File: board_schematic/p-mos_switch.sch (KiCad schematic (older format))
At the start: 5 parts

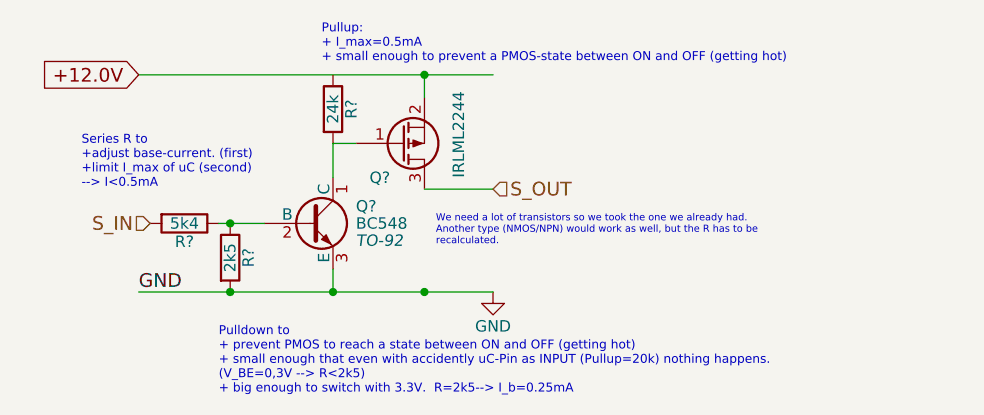
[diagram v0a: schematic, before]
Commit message: V0.2.1: First schematic for BOM
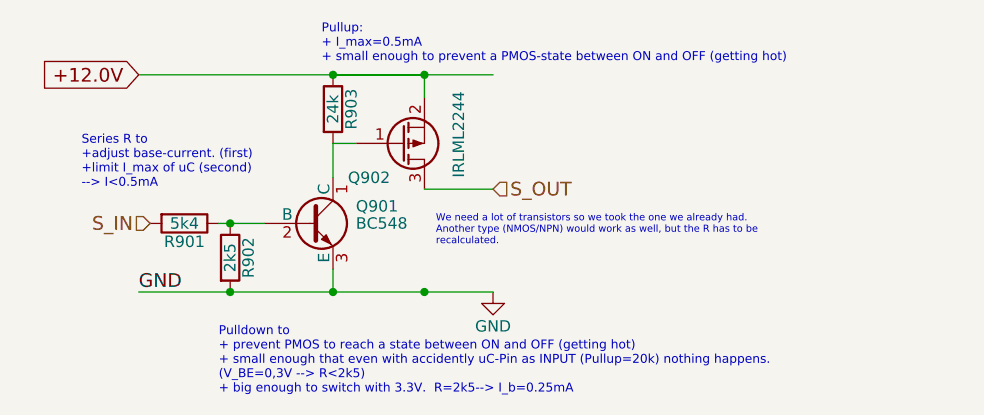
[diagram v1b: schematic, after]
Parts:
- Q301: renamed from Q?; footprint TO-92 -> project_footprints:TO-92_Molded_0.6space_Oval
- Q302: renamed from Q?; footprint (none) -> TO_SOT_Packages_SMD:SOT-23_Handsoldering
- gave numbers to parts that had none: 3
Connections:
- wire segments 8 -> 9
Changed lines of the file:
@@
 $EndDescr
 $Comp
-L BC548 Q?
+L BC548 Q301
 U 1 1 572887A4
 P 3100 1900
-AR Path="/572753D2/572887A4" Ref="Q?"  Part="1"
-AR Path="/572880E3/572887A4" Ref="Q?"  Part="1"
-AR Path="/57276127/572887A4" Ref="Q?"  Part="1"
-AR Path="/57275FE1/572887A4" Ref="Q?"  Part="1"
-AR Path="/57276E10/572887A4" Ref="Q?"  Part="1"
-AR Path="/57276A8A/572887A4" Ref="Q?"  Part="1"
-AR Path="/5727C617/572887A4" Ref="Q?"  Part="1"
-AR Path="/5727C61F/572887A4" Ref="Q?"  Part="1"
-F 0 "Q?" H 3300 1975 50  0000 L CNN
+AR Path="/572880E3/572887A4" Ref="Q301"  Part="1"
+AR Path="/572753D2/572887A4" Ref="Q401"  Part="1"
+AR Path="/57275FE1/572887A4" Ref="Q501"  Part="1"
+AR Path="/57276A86/572887A4" Ref="Q601"  Part="1"
+AR Path="/57276A8A/572887A4" Ref="Q701"  Part="1"
+AR Path="/57276A8E/572887A4" Ref="Q801"  Part="1"
+AR Path="/57276E10/572887A4" Ref="Q901"  Part="1"
+AR Path="/5727C603/572887A4" Ref="Q1001"  Part="1"
+AR Path="/5727C607/572887A4" Ref="Q1101"  Part="1"
+AR Path="/5727C60B/572887A4" Ref="Q1201"  Part="1"
+AR Path="/5727C60F/572887A4" Ref="Q1301"  Part="1"
+AR Path="/5727C613/572887A4" Ref="Q1401"  Part="1"
+AR Path="/5727C617/572887A4" Ref="Q1501"  Part="1"
+AR Path="/5727C61B/572887A4" Ref="Q1601"  Part="1"
+F 0 "Q901" H 3300 1975 50  0000 L CNN
 F 1 "BC548" H 3300 1900 50  0000 L CNN
-F 2 "TO-92" H 3300 1825 50  0000 L CIN
+F 2 "project_footprints:TO-92_Molded_0.6space_Oval" H 3300 1825 50  0001 L CIN
 F 3 "" H 3100 1900 50  0000 L CNN
 	1    3100 1900
@@
 $EndComp
 $Comp
-L Q_PMOS_GSD Q?
+L Q_PMOS_GSD Q302
 U 1 1 57288D4B
 P 3500 1550
-AR Path="/572753D2/57288D4B" Ref="Q?"  Part="1"
-AR Path="/572880E3/57288D4B" Ref="Q?"  Part="1"
-AR Path="/57276127/57288D4B" Ref="Q?"  Part="1"
-AR Path="/57275FE1/57288D4B" Ref="Q?"  Part="1"
-AR Path="/57276E10/57288D4B" Ref="Q?"  Part="1"
-AR Path="/57276A8A/57288D4B" Ref="Q?"  Part="1"
-AR Path="/5727C617/57288D4B" Ref="Q?"  Part="1"
-AR Path="/5727C61F/57288D4B" Ref="Q?"  Part="1"
-F 0 "Q?" H 3450 1700 50  0000 R CNN
+AR Path="/572880E3/57288D4B" Ref="Q302"  Part="1"
+AR Path="/572753D2/57288D4B" Ref="Q402"  Part="1"
+AR Path="/57275FE1/57288D4B" Ref="Q502"  Part="1"
+AR Path="/57276A86/57288D4B" Ref="Q602"  Part="1"
+AR Path="/57276A8A/57288D4B" Ref="Q702"  Part="1"
+AR Path="/57276A8E/57288D4B" Ref="Q802"  Part="1"
+AR Path="/57276E10/57288D4B" Ref="Q902"  Part="1"
+AR Path="/5727C603/57288D4B" Ref="Q1002"  Part="1"
+AR Path="/5727C607/57288D4B" Ref="Q1102"  Part="1"
+AR Path="/5727C60B/57288D4B" Ref="Q1202"  Part="1"
+AR Path="/5727C60F/57288D4B" Ref="Q1302"  Part="1"
+AR Path="/5727C613/57288D4B" Ref="Q1402"  Part="1"
+AR Path="/5727C617/57288D4B" Ref="Q1502"  Part="1"
+AR Path="/5727C61B/57288D4B" Ref="Q1602"  Part="1"
+F 0 "Q902" H 3450 1700 50  0000 R CNN
 F 1 "IRLML2244" V 3750 1700 50  0000 R CNN
-F 2 "" H 3700 1650 50  0000 C CNN
+F 2 "TO_SOT_Packages_SMD:SOT-23_Handsoldering" H 3700 1650 50  0001 C CNN
 F 3 "" H 3500 1550 50  0000 C CNN
 	1    3500 1550
@@
 $EndComp
 $Comp
-L R R?
+L R R302
 U 1 1 57288EBC
 P 2750 2050
-AR Path="/572753D2/57288EBC" Ref="R?"  Part="1"
-AR Path="/572880E3/57288EBC" Ref="R?"  Part="1"
-AR Path="/57276127/57288EBC" Ref="R?"  Part="1"
-AR Path="/57275FE1/57288EBC" Ref="R?"  Part="1"
-AR Path="/57276E10/57288EBC" Ref="R?"  Part="1"
-AR Path="/57276A8A/57288EBC" Ref="R?"  Part="1"
-AR Path="/5727C617/57288EBC" Ref="R?"  Part="1"
-AR Path="/5727C61F/57288EBC" Ref="R?"  Part="1"
-F 0 "R?" V 2830 2050 50  0000 C CNN
+AR Path="/572880E3/57288EBC" Ref="R302"  Part="1"
+AR Path="/572753D2/57288EBC" Ref="R402"  Part="1"
+AR Path="/57275FE1/57288EBC" Ref="R502"  Part="1"
+AR Path="/57276A86/57288EBC" Ref="R602"  Part="1"
+AR Path="/57276A8A/57288EBC" Ref="R702"  Part="1"
+AR Path="/57276A8E/57288EBC" Ref="R802"  Part="1"
+AR Path="/57276E10/57288EBC" Ref="R902"  Part="1"
+AR Path="/5727C603/57288EBC" Ref="R1002"  Part="1"
+AR Path="/5727C607/57288EBC" Ref="R1102"  Part="1"
+AR Path="/5727C60B/57288EBC" Ref="R1202"  Part="1"
+AR Path="/5727C60F/57288EBC" Ref="R1302"  Part="1"
+AR Path="/5727C613/57288EBC" Ref="R1402"  Part="1"
+AR Path="/5727C617/57288EBC" Ref="R1502"  Part="1"
+AR Path="/5727C61B/57288EBC" Ref="R1602"  Part="1"
+F 0 "R902" V 2830 2050 50  0000 C CNN
 F 1 "2k5" V 2750 2050 50  0000 C CNN
 F 2 "Resistors_SMD:R_0805_HandSoldering" V 2680 2050 50  0001 C CNN
@@
 $EndComp
 $Comp
-L R R?
+L R R303
 U 1 1 57288ED3
 P 3200 1400
-AR Path="/572753D2/57288ED3" Ref="R?"  Part="1"
-AR Path="/572880E3/57288ED3" Ref="R?"  Part="1"
-AR Path="/57276127/57288ED3" Ref="R?"  Part="1"
-AR Path="/57275FE1/57288ED3" Ref="R?"  Part="1"
-AR Path="/57276E10/57288ED3" Ref="R?"  Part="1"
-AR Path="/57276A8A/57288ED3" Ref="R?"  Part="1"
-AR Path="/5727C617/57288ED3" Ref="R?"  Part="1"
-AR Path="/5727C61F/57288ED3" Ref="R?"  Part="1"
-F 0 "R?" V 3280 1400 50  0000 C CNN
+AR Path="/572880E3/57288ED3" Ref="R303"  Part="1"
+AR Path="/572753D2/57288ED3" Ref="R403"  Part="1"
+AR Path="/57275FE1/57288ED3" Ref="R503"  Part="1"
+AR Path="/57276A86/57288ED3" Ref="R603"  Part="1"
+AR Path="/57276A8A/57288ED3" Ref="R703"  Part="1"
+AR Path="/57276A8E/57288ED3" Ref="R803"  Part="1"
+AR Path="/57276E10/57288ED3" Ref="R903"  Part="1"
+AR Path="/5727C603/57288ED3" Ref="R1003"  Part="1"
+AR Path="/5727C607/57288ED3" Ref="R1103"  Part="1"
+AR Path="/5727C60B/57288ED3" Ref="R1203"  Part="1"
+AR Path="/5727C60F/57288ED3" Ref="R1303"  Part="1"
+AR Path="/5727C613/57288ED3" Ref="R1403"  Part="1"
+AR Path="/5727C617/57288ED3" Ref="R1503"  Part="1"
+AR Path="/5727C61B/57288ED3" Ref="R1603"  Part="1"
+F 0 "R903" V 3280 1400 50  0000 C CNN
 F 1 "24k" V 3200 1400 50  0000 C CNN
 F 2 "Resistors_SMD:R_0805_HandSoldering" V 3130 1400 50  0001 C CNN
@@
 We need a lot of transistors so we took the one we already had.\nAnother type (NMOS/NPN) would work as well, but the R has to be\nrecalculated.
 $Comp
-L R R?
+L R R301
 U 1 1 57270EA2
 P 2550 1900
-AR Path="/572753D2/57270EA2" Ref="R?"  Part="1"
-AR Path="/572880E3/57270EA2" Ref="R?"  Part="1"
-AR Path="/57276127/57270EA2" Ref="R?"  Part="1"
-AR Path="/57275FE1/57270EA2" Ref="R?"  Part="1"
-AR Path="/57276E10/57270EA2" Ref="R?"  Part="1"
-AR Path="/57276A8A/57270EA2" Ref="R?"  Part="1"
-AR Path="/5727C617/57270EA2" Ref="R?"  Part="1"
-AR Path="/5727C61F/57270EA2" Ref="R?"  Part="1"
-F 0 "R?" V 2630 1900 50  0000 C CNN
+AR Path="/572880E3/57270EA2" Ref="R301"  Part="1"
+AR Path="/572753D2/57270EA2" Ref="R401"  Part="1"
+AR Path="/57275FE1/57270EA2" Ref="R501"  Part="1"
+AR Path="/57276A86/57270EA2" Ref="R601"  Part="1"
+AR Path="/57276A8A/57270EA2" Ref="R701"  Part="1"
+AR Path="/57276A8E/57270EA2" Ref="R801"  Part="1"
+AR Path="/57276E10/57270EA2" Ref="R901"  Part="1"
+AR Path="/5727C603/57270EA2" Ref="R1001"  Part="1"
+AR Path="/5727C607/57270EA2" Ref="R1101"  Part="1"
+AR Path="/5727C60B/57270EA2" Ref="R1201"  Part="1"
+AR Path="/5727C60F/57270EA2" Ref="R1301"  Part="1"
+AR Path="/5727C613/57270EA2" Ref="R1401"  Part="1"
+AR Path="/5727C617/57270EA2" Ref="R1501"  Part="1"
+AR Path="/5727C61B/57270EA2" Ref="R1601"  Part="1"
+F 0 "R901" V 2630 1900 50  0000 C CNN
 F 1 "5k4" V 2550 1900 50  0000 C CNN
 F 2 "Resistors_SMD:R_0805_HandSoldering" V 2480 1900 50  0001 C CNN
@@
 $EndComp
 $Comp
-L GND #PWR?
+L GND #PWR08
 U 1 1 572710CE
 P 3900 2200
-AR Path="/572753D2/572710CE" Ref="#PWR?"  Part="1"
-AR Path="/572880E3/572710CE" Ref="#PWR?"  Part="1"
-AR Path="/57276127/572710CE" Ref="#PWR?"  Part="1"
-AR Path="/57275FE1/572710CE" Ref="#PWR?"  Part="1"
-AR Path="/57276E10/572710CE" Ref="#PWR?"  Part="1"
-AR Path="/57276A8A/572710CE" Ref="#PWR?"  Part="1"
-AR Path="/5727C617/572710CE" Ref="#PWR?"  Part="1"
-AR Path="/5727C61F/572710CE" Ref="#PWR?"  Part="1"
-F 0 "#PWR?" H 3900 1950 50  0001 C CNN
+AR Path="/572880E3/572710CE" Ref="#PWR08"  Part="1"
+AR Path="/572753D2/572710CE" Ref="#PWR09"  Part="1"
+AR Path="/57275FE1/572710CE" Ref="#PWR010"  Part="1"
+AR Path="/57276A86/572710CE" Ref="#PWR011"  Part="1"
+AR Path="/57276A8A/572710CE" Ref="#PWR012"  Part="1"
+AR Path="/57276A8E/572710CE" Ref="#PWR013"  Part="1"
+AR Path="/57276E10/572710CE" Ref="#PWR014"  Part="1"
+AR Path="/5727C603/572710CE" Ref="#PWR015"  Part="1"
+AR Path="/5727C607/572710CE" Ref="#PWR016"  Part="1"
+AR Path="/5727C60B/572710CE" Ref="#PWR017"  Part="1"
+AR Path="/5727C60F/572710CE" Ref="#PWR018"  Part="1"
+AR Path="/5727C613/572710CE" Ref="#PWR019"  Part="1"
+AR Path="/5727C617/572710CE" Ref="#PWR020"  Part="1"
+AR Path="/5727C61B/572710CE" Ref="#PWR021"  Part="1"
+F 0 "#PWR014" H 3900 1950 50  0001 C CNN
 F 1 "GND" H 3900 2050 50  0000 C CNN
 F 2 "" H 3900 2200 50  0000 C CNN
@@
 Text Notes 3150 1200 0    39   ~ 0
 Pullup: \n+ I_max=0.5mA\n+ small enough to prevent a PMOS-state between ON and OFF (getting hot)
+Wire Wire Line
+	3600 1250 3200 1250
+Connection ~ 3200 1250
 $EndSCHEMATC

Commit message: V0.3.1: First layout
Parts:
- R301: renamed from R303; value 24k -> 27k
- R302: renamed from R301; value 5k4 -> 5k6
- R303: renamed from R302; value 2k5 -> 2k7
- renumbered Q302 to Q301, Q301 to Q302
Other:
- note added: "Pulldown to \n+ prevent PMOS to reach a state between ON and OFF (getting hot)\n+ small enough that even with accidently uC-Pin as INPUT (Pullup=20k) nothing happens.\n(V_BE=0,3V --> R<2k7)\n+ big enough to switch with 3.3V. R=2k7--> I_b=0.26mA"
- note removed: "Pulldown to \n+ prevent PMOS to reach a state between ON and OFF (getting hot)\n+ small enough that even with accidently uC-Pin as INPUT (Pullup=20k) nothing happens.\n(V_BE=0,3V --> R<2k5)\n+ big enough to switch with 3.3V. R=2k5--> I_b=0.25mA"
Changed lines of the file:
@@
 $Descr A4 11693 8268
 encoding utf-8
-Sheet 9 16
-Title ""
-Date ""
-Rev ""
+Sheet 3 16
+Title "uC_segment_control"
+Date "2016-05-10"
+Rev "V0.3.1"
 Comp ""
 Comment1 ""
@@
 $EndDescr
 $Comp
-L BC548 Q301
+L BC548 Q302
 U 1 1 572887A4
 P 3100 1900
-AR Path="/572880E3/572887A4" Ref="Q301"  Part="1"
-AR Path="/572753D2/572887A4" Ref="Q401"  Part="1"
-AR Path="/57275FE1/572887A4" Ref="Q501"  Part="1"
-AR Path="/57276A86/572887A4" Ref="Q601"  Part="1"
-AR Path="/57276A8A/572887A4" Ref="Q701"  Part="1"
-AR Path="/57276A8E/572887A4" Ref="Q801"  Part="1"
-AR Path="/57276E10/572887A4" Ref="Q901"  Part="1"
-AR Path="/5727C603/572887A4" Ref="Q1001"  Part="1"
-AR Path="/5727C607/572887A4" Ref="Q1101"  Part="1"
-AR Path="/5727C60B/572887A4" Ref="Q1201"  Part="1"
-AR Path="/5727C60F/572887A4" Ref="Q1301"  Part="1"
-AR Path="/5727C613/572887A4" Ref="Q1401"  Part="1"
-AR Path="/5727C617/572887A4" Ref="Q1501"  Part="1"
-AR Path="/5727C61B/572887A4" Ref="Q1601"  Part="1"
-F 0 "Q901" H 3300 1975 50  0000 L CNN
+AR Path="/572880E3/572887A4" Ref="Q302"  Part="1"
+AR Path="/572753D2/572887A4" Ref="Q402"  Part="1"
+AR Path="/57275FE1/572887A4" Ref="Q502"  Part="1"
+AR Path="/57276A86/572887A4" Ref="Q602"  Part="1"
+AR Path="/57276A8A/572887A4" Ref="Q702"  Part="1"
+AR Path="/57276A8E/572887A4" Ref="Q802"  Part="1"
+AR Path="/57276E10/572887A4" Ref="Q902"  Part="1"
+AR Path="/5727C603/572887A4" Ref="Q1002"  Part="1"
+AR Path="/5727C607/572887A4" Ref="Q1102"  Part="1"
+AR Path="/5727C60B/572887A4" Ref="Q1202"  Part="1"
+AR Path="/5727C60F/572887A4" Ref="Q1302"  Part="1"
+AR Path="/5727C613/572887A4" Ref="Q1402"  Part="1"
+AR Path="/5727C617/572887A4" Ref="Q1502"  Part="1"
+AR Path="/5727C61B/572887A4" Ref="Q1602"  Part="1"
+F 0 "Q302" H 3300 1975 50  0000 L CNN
 F 1 "BC548" H 3300 1900 50  0000 L CNN
 F 2 "project_footprints:TO-92_Molded_0.6space_Oval" H 3300 1825 50  0001 L CIN
@@
 $EndComp
 $Comp
-L Q_PMOS_GSD Q302
+L Q_PMOS_GSD Q301
 U 1 1 57288D4B
 P 3500 1550
-AR Path="/572880E3/57288D4B" Ref="Q302"  Part="1"
-AR Path="/572753D2/57288D4B" Ref="Q402"  Part="1"
-AR Path="/57275FE1/57288D4B" Ref="Q502"  Part="1"
-AR Path="/57276A86/57288D4B" Ref="Q602"  Part="1"
-AR Path="/57276A8A/57288D4B" Ref="Q702"  Part="1"
-AR Path="/57276A8E/57288D4B" Ref="Q802"  Part="1"
-AR Path="/57276E10/57288D4B" Ref="Q902"  Part="1"
-AR Path="/5727C603/57288D4B" Ref="Q1002"  Part="1"
-AR Path="/5727C607/57288D4B" Ref="Q1102"  Part="1"
-AR Path="/5727C60B/57288D4B" Ref="Q1202"  Part="1"
-AR Path="/5727C60F/57288D4B" Ref="Q1302"  Part="1"
-AR Path="/5727C613/57288D4B" Ref="Q1402"  Part="1"
-AR Path="/5727C617/57288D4B" Ref="Q1502"  Part="1"
-AR Path="/5727C61B/57288D4B" Ref="Q1602"  Part="1"
-F 0 "Q902" H 3450 1700 50  0000 R CNN
+AR Path="/572880E3/57288D4B" Ref="Q301"  Part="1"
+AR Path="/572753D2/57288D4B" Ref="Q401"  Part="1"
+AR Path="/57275FE1/57288D4B" Ref="Q501"  Part="1"
+AR Path="/57276A86/57288D4B" Ref="Q601"  Part="1"
+AR Path="/57276A8A/57288D4B" Ref="Q701"  Part="1"
+AR Path="/57276A8E/57288D4B" Ref="Q801"  Part="1"
+AR Path="/57276E10/57288D4B" Ref="Q901"  Part="1"
+AR Path="/5727C603/57288D4B" Ref="Q1001"  Part="1"
+AR Path="/5727C607/57288D4B" Ref="Q1101"  Part="1"
+AR Path="/5727C60B/57288D4B" Ref="Q1201"  Part="1"
+AR Path="/5727C60F/57288D4B" Ref="Q1301"  Part="1"
+AR Path="/5727C613/57288D4B" Ref="Q1401"  Part="1"
+AR Path="/5727C617/57288D4B" Ref="Q1501"  Part="1"
+AR Path="/5727C61B/57288D4B" Ref="Q1601"  Part="1"
+F 0 "Q301" H 3450 1700 50  0000 R CNN
 F 1 "IRLML2244" V 3750 1700 50  0000 R CNN
 F 2 "TO_SOT_Packages_SMD:SOT-23_Handsoldering" H 3700 1650 50  0001 C CNN
@@
 $EndComp
 $Comp
-L R R302
+L R R303
 U 1 1 57288EBC
 P 2750 2050
-AR Path="/572880E3/57288EBC" Ref="R302"  Part="1"
-AR Path="/572753D2/57288EBC" Ref="R402"  Part="1"
-AR Path="/57275FE1/57288EBC" Ref="R502"  Part="1"
-AR Path="/57276A86/57288EBC" Ref="R602"  Part="1"
-AR Path="/57276A8A/57288EBC" Ref="R702"  Part="1"
-AR Path="/57276A8E/57288EBC" Ref="R802"  Part="1"
-AR Path="/57276E10/57288EBC" Ref="R902"  Part="1"
-AR Path="/5727C603/57288EBC" Ref="R1002"  Part="1"
-AR Path="/5727C607/57288EBC" Ref="R1102"  Part="1"
-AR Path="/5727C60B/57288EBC" Ref="R1202"  Part="1"
-AR Path="/5727C60F/57288EBC" Ref="R1302"  Part="1"
-AR Path="/5727C613/57288EBC" Ref="R1402"  Part="1"
-AR Path="/5727C617/57288EBC" Ref="R1502"  Part="1"
-AR Path="/5727C61B/57288EBC" Ref="R1602"  Part="1"
-F 0 "R902" V 2830 2050 50  0000 C CNN
-F 1 "2k5" V 2750 2050 50  0000 C CNN
+AR Path="/572880E3/57288EBC" Ref="R303"  Part="1"
+AR Path="/572753D2/57288EBC" Ref="R403"  Part="1"
+AR Path="/57275FE1/57288EBC" Ref="R503"  Part="1"
+AR Path="/57276A86/57288EBC" Ref="R603"  Part="1"
+AR Path="/57276A8A/57288EBC" Ref="R703"  Part="1"
+AR Path="/57276A8E/57288EBC" Ref="R803"  Part="1"
+AR Path="/57276E10/57288EBC" Ref="R903"  Part="1"
+AR Path="/5727C603/57288EBC" Ref="R1003"  Part="1"
+AR Path="/5727C607/57288EBC" Ref="R1103"  Part="1"
+AR Path="/5727C60B/57288EBC" Ref="R1203"  Part="1"
+AR Path="/5727C60F/57288EBC" Ref="R1303"  Part="1"
+AR Path="/5727C613/57288EBC" Ref="R1403"  Part="1"
+AR Path="/5727C617/57288EBC" Ref="R1503"  Part="1"
+AR Path="/5727C61B/57288EBC" Ref="R1603"  Part="1"
+F 0 "R303" V 2830 2050 50  0000 C CNN
+F 1 "2k7" V 2750 2050 50  0000 C CNN
 F 2 "Resistors_SMD:R_0805_HandSoldering" V 2680 2050 50  0001 C CNN
 F 3 "" H 2750 2050 50  0000 C CNN
@@
 $EndComp
 $Comp
-L R R303
+L R R301
 U 1 1 57288ED3
 P 3200 1400
-AR Path="/572880E3/57288ED3" Ref="R303"  Part="1"
-AR Path="/572753D2/57288ED3" Ref="R403"  Part="1"
-AR Path="/57275FE1/57288ED3" Ref="R503"  Part="1"
-AR Path="/57276A86/57288ED3" Ref="R603"  Part="1"
-AR Path="/57276A8A/57288ED3" Ref="R703"  Part="1"
-AR Path="/57276A8E/57288ED3" Ref="R803"  Part="1"
-AR Path="/57276E10/57288ED3" Ref="R903"  Part="1"
-AR Path="/5727C603/57288ED3" Ref="R1003"  Part="1"
-AR Path="/5727C607/57288ED3" Ref="R1103"  Part="1"
-AR Path="/5727C60B/57288ED3" Ref="R1203"  Part="1"
-AR Path="/5727C60F/57288ED3" Ref="R1303"  Part="1"
-AR Path="/5727C613/57288ED3" Ref="R1403"  Part="1"
-AR Path="/5727C617/57288ED3" Ref="R1503"  Part="1"
-AR Path="/5727C61B/57288ED3" Ref="R1603"  Part="1"
-F 0 "R903" V 3280 1400 50  0000 C CNN
-F 1 "24k" V 3200 1400 50  0000 C CNN
+AR Path="/572880E3/57288ED3" Ref="R301"  Part="1"
+AR Path="/572753D2/57288ED3" Ref="R401"  Part="1"
+AR Path="/57275FE1/57288ED3" Ref="R501"  Part="1"
+AR Path="/57276A86/57288ED3" Ref="R601"  Part="1"
+AR Path="/57276A8A/57288ED3" Ref="R701"  Part="1"
+AR Path="/57276A8E/57288ED3" Ref="R801"  Part="1"
+AR Path="/57276E10/57288ED3" Ref="R901"  Part="1"
+AR Path="/5727C603/57288ED3" Ref="R1001"  Part="1"
+AR Path="/5727C607/57288ED3" Ref="R1101"  Part="1"
+AR Path="/5727C60B/57288ED3" Ref="R1201"  Part="1"
+AR Path="/5727C60F/57288ED3" Ref="R1301"  Part="1"
+AR Path="/5727C613/57288ED3" Ref="R1401"  Part="1"
+AR Path="/5727C617/57288ED3" Ref="R1501"  Part="1"
+AR Path="/5727C61B/57288ED3" Ref="R1601"  Part="1"
+F 0 "R301" V 3280 1400 50  0000 C CNN
+F 1 "27k" V 3200 1400 50  0000 C CNN
 F 2 "Resistors_SMD:R_0805_HandSoldering" V 3130 1400 50  0001 C CNN
 F 3 "" H 3200 1400 50  0000 C CNN
@@
 $EndComp
 Text Notes 2700 2650 0    39   ~ 0
-Pulldown to \n+ prevent PMOS to reach a state between ON and OFF (getting hot)\n+ small enough that even with accidently uC-Pin as INPUT (Pullup=20k) nothing happens.\n(V_BE=0,3V --> R<2k5)\n+ big enough to switch with 3.3V.  R=2k5--> I_b=0.25mA
+Pulldown to \n+ prevent PMOS to reach a state between ON and OFF (getting hot)\n+ small enough that even with accidently uC-Pin as INPUT (Pullup=20k) nothing happens.\n(V_BE=0,3V --> R<2k7)\n+ big enough to switch with 3.3V.  R=2k7--> I_b=0.26mA
 Text Notes 3650 2000 0    31   ~ 0
 We need a lot of transistors so we took the one we already had.\nAnother type (NMOS/NPN) would work as well, but the R has to be\nrecalculated.
 $Comp
-L R R301
+L R R302
 U 1 1 57270EA2
 P 2550 1900
-AR Path="/572880E3/57270EA2" Ref="R301"  Part="1"
-AR Path="/572753D2/57270EA2" Ref="R401"  Part="1"
-AR Path="/57275FE1/57270EA2" Ref="R501"  Part="1"
-AR Path="/57276A86/57270EA2" Ref="R601"  Part="1"
-AR Path="/57276A8A/57270EA2" Ref="R701"  Part="1"
-AR Path="/57276A8E/57270EA2" Ref="R801"  Part="1"
-AR Path="/57276E10/57270EA2" Ref="R901"  Part="1"
-AR Path="/5727C603/57270EA2" Ref="R1001"  Part="1"
-AR Path="/5727C607/57270EA2" Ref="R1101"  Part="1"
-AR Path="/5727C60B/57270EA2" Ref="R1201"  Part="1"
-AR Path="/5727C60F/57270EA2" Ref="R1301"  Part="1"
-AR Path="/5727C613/57270EA2" Ref="R1401"  Part="1"
-AR Path="/5727C617/57270EA2" Ref="R1501"  Part="1"
-AR Path="/5727C61B/57270EA2" Ref="R1601"  Part="1"
-F 0 "R901" V 2630 1900 50  0000 C CNN
-F 1 "5k4" V 2550 1900 50  0000 C CNN
+AR Path="/572880E3/57270EA2" Ref="R302"  Part="1"
+AR Path="/572753D2/57270EA2" Ref="R402"  Part="1"
+AR Path="/57275FE1/57270EA2" Ref="R502"  Part="1"
+AR Path="/57276A86/57270EA2" Ref="R602"  Part="1"
+AR Path="/57276A8A/57270EA2" Ref="R702"  Part="1"
+AR Path="/57276A8E/57270EA2" Ref="R802"  Part="1"
+AR Path="/57276E10/57270EA2" Ref="R902"  Part="1"
+AR Path="/5727C603/57270EA2" Ref="R1002"  Part="1"
+AR Path="/5727C607/57270EA2" Ref="R1102"  Part="1"
+AR Path="/5727C60B/57270EA2" Ref="R1202"  Part="1"
+AR Path="/5727C60F/57270EA2" Ref="R1302"  Part="1"
+AR Path="/5727C613/57270EA2" Ref="R1402"  Part="1"
+AR Path="/5727C617/57270EA2" Ref="R1502"  Part="1"
+AR Path="/5727C61B/57270EA2" Ref="R1602"  Part="1"
+F 0 "R302" V 2630 1900 50  0000 C CNN
+F 1 "5k6" V 2550 1900 50  0000 C CNN
 F 2 "Resistors_SMD:R_0805_HandSoldering" V 2480 1900 50  0001 C CNN
 F 3 "" H 2550 1900 50  0000 C CNN
@@
 AR Path="/5727C617/572710CE" Ref="#PWR020"  Part="1"
 AR Path="/5727C61B/572710CE" Ref="#PWR021"  Part="1"
-F 0 "#PWR014" H 3900 1950 50  0001 C CNN
+F 0 "#PWR08" H 3900 1950 50  0001 C CNN
 F 1 "GND" H 3900 2050 50  0000 C CNN
 F 2 "" H 3900 2200 50  0000 C CNN
